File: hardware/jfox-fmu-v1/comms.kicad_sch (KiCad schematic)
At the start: 6 parts, among them J30 USB-C, J31 microSD, U30 TCAN332, U31 TCAN332

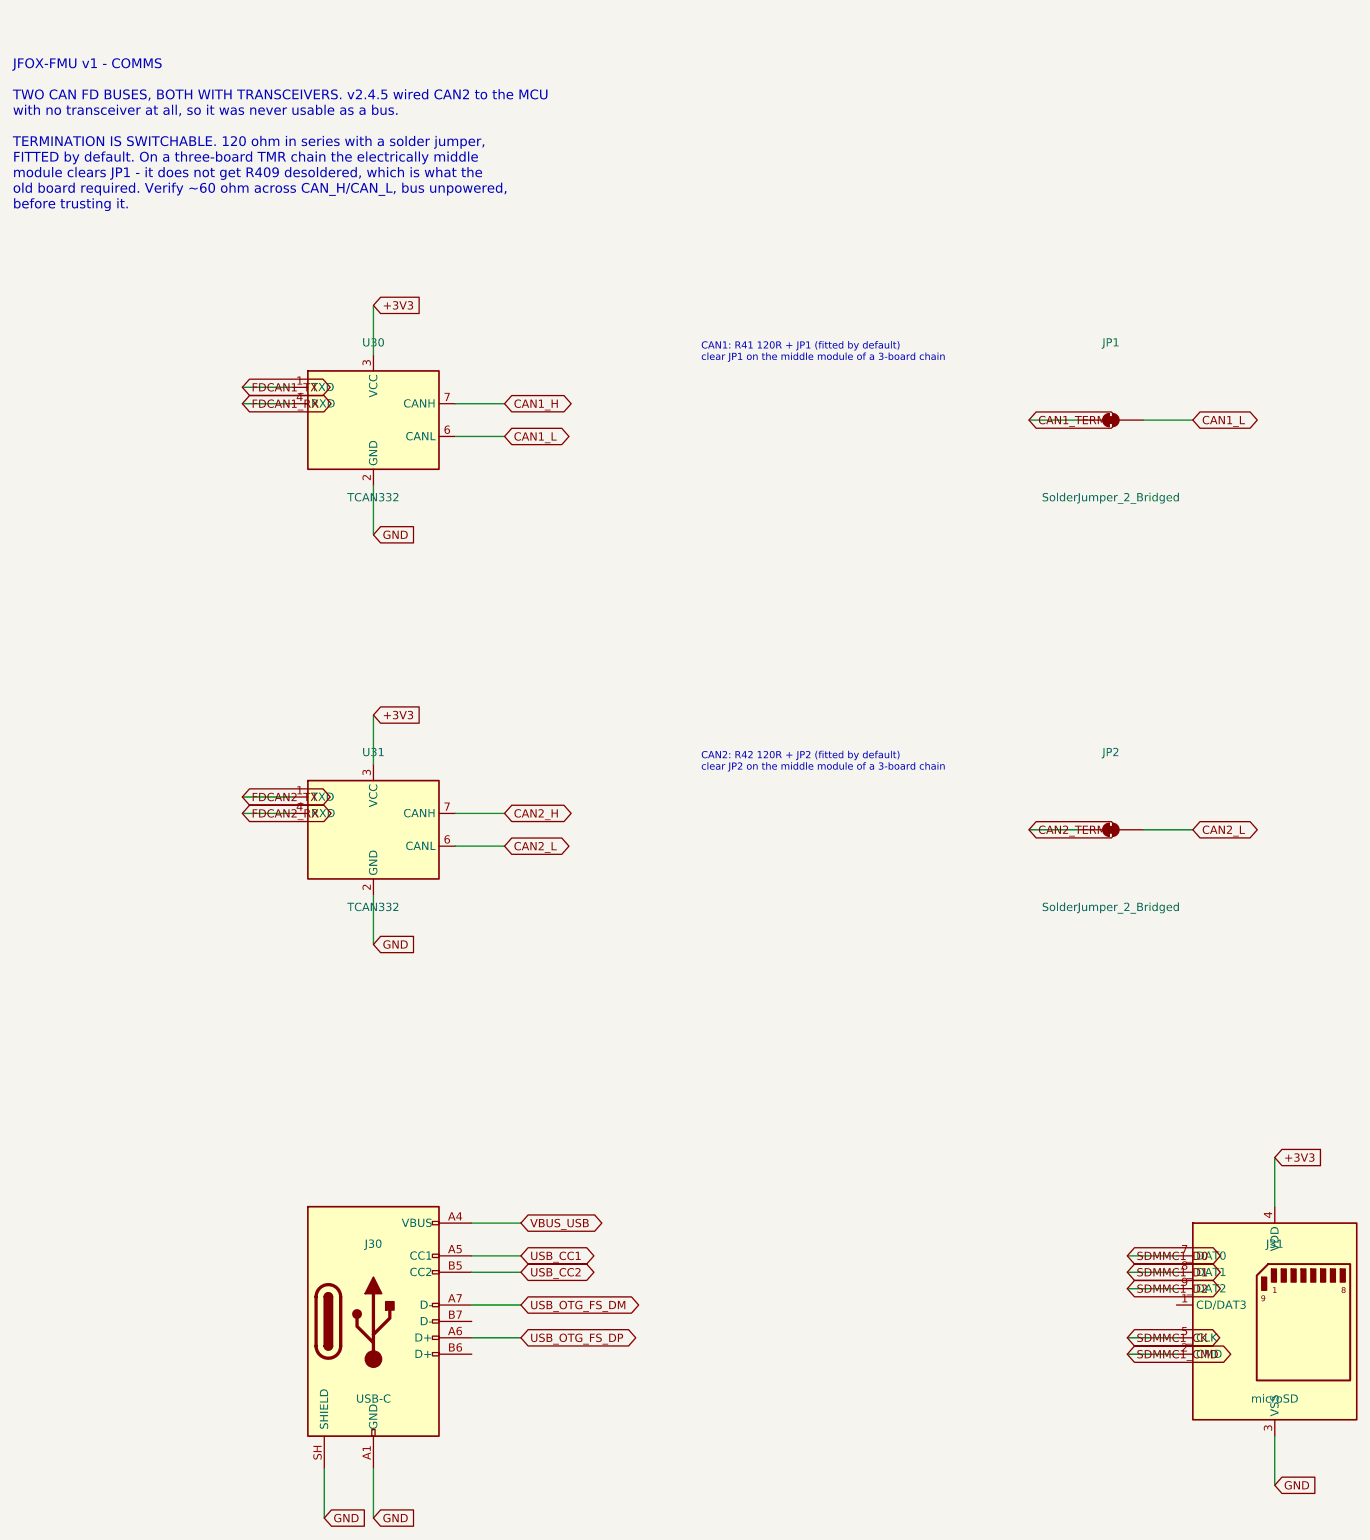
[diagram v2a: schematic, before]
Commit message: A4 title-blocked sheets, and the 25 power pins that were never wired
Every sheet now carries a title block naming JFOX Aircraft Co., Ltd., with a
per-sheet title, revision, date and the notes that used to float as loose text.

A4 PORTRAIT, not landscape, and not by preference. The STM32H753IITx symbol is
a single unit - KiCad's library gives it only _0_1 body and _1_1 pin
sub-symbols, so it cannot be split across pages - and its 176 pins span
231.1 mm. A4 landscape offers about 180 mm of usable height and would cut the
MCU in half. Portrait offers 237 mm. The part fits with 2 mm to spare, which
is why the page margin is 2 mm: it is the largest margin that still holds an
LQFP176, not a number chosen for looks.

The frame geometry was measured, not assumed - an empty A4 portrait sheet
plotted through kicad-cli, frame read off the SVG at 12,12 -> 198,285 with the
title block claiming x >= 90, y >= 253.

Three defects the work surfaced, in rising order of how much they mattered:

Every sheet had content at negative coordinates, off the page entirely, where
KiCad edits it happily and the plotter crops it away. Nothing had complained
because nothing was looking. fit() now translates each sheet into the drawable
area and refuses - loudly - to emit one that does not fit, because a schematic
that is silently cropped lies about the board.

fit() then passed the power sheet while its rightmost label sat 8.6 mm past
the frame. A global label's angle is the direction its CONNECTION faces, so
the text runs the opposite way; reading it the intuitive way put every
estimated extent on the wrong side of its anchor. That is worse than not
estimating: it reports "inside the frame" precisely when labels hang off it.
Caught by measuring KiCad's own plotted geometry instead of trusting the
estimate - which is what check_fmu_sheets.py now does on every sheet, with
--exclude-drawing-sheet so only the circuit is measured.

And centring the sheets by (SAFE_W - w) / 2 shifted every wire off th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
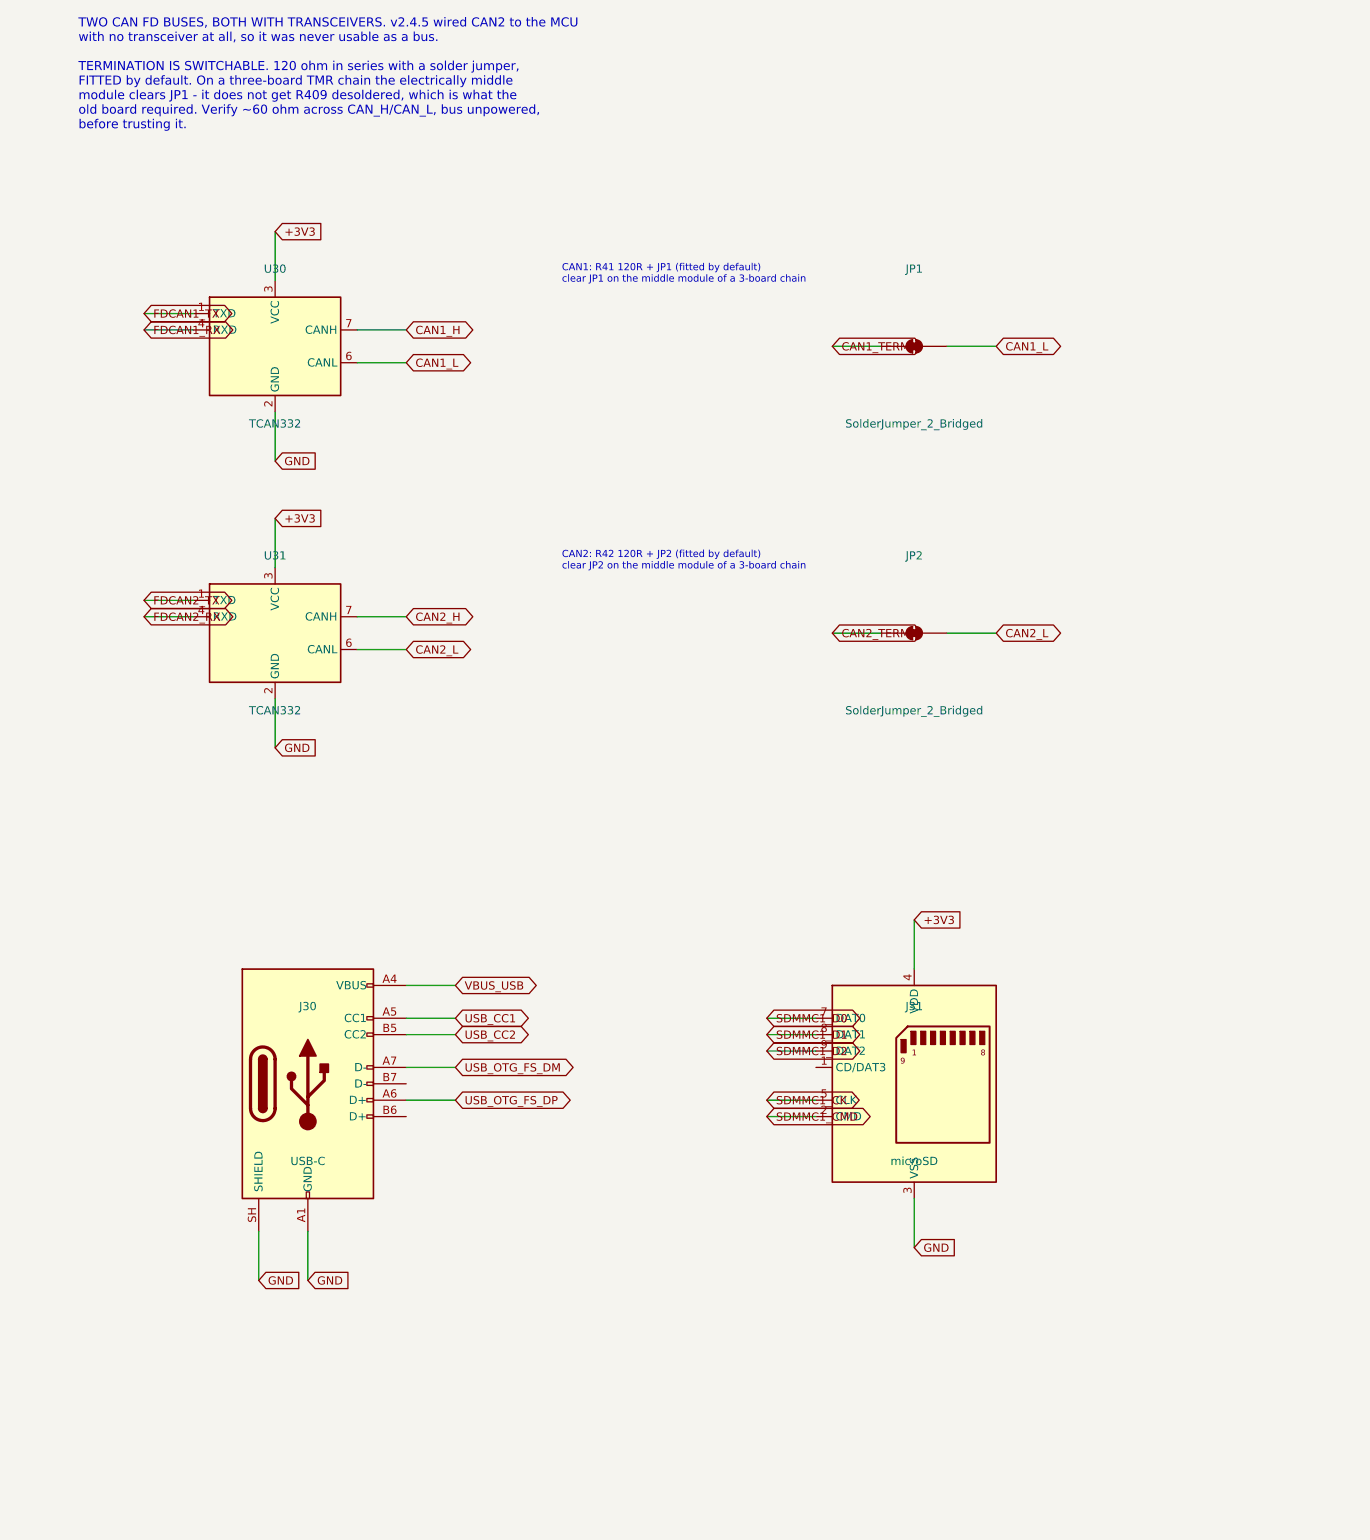
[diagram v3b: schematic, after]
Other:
- note added: "TWO CAN FD BUSES, BOTH WITH TRANSCEIVERS. v2.4.5 wired CAN2 to the MCU with no transceiver at all, so it was never usable as a bus. TERMINATION IS SWITCHABLE. 120 ohm in series with a solder jumper, FITTED by default. On a three-board TMR chain the electrically middle module clears JP1 - it does not get R409 desoldered, which is what the old board required. Verify ~60 ohm across CAN_H/CAN_L, bus 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"
- note removed: "JFOX-FMU v1 - COMMS TWO CAN FD BUSES, BOTH WITH TRANSCEIVERS. v2.4.5 wired CAN2 to the MCU with no transceiver at all, so it was never usable as a bus. TERMINATION IS SWITCHABLE. 120 ohm in series with a solder jumper, FITTED by default. On a three-board TMR chain the electrically middle module clears JP1 - it does not get R409 desoldered, which is what the old board required. Verify ~60 ohm acro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"
- company: (none) -> JFOX Aircraft Co., Ltd.
- title: (none) -> Comms and Storage

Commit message: Footprint every part, and verify each one exists
58 of 58 components now carry a footprint chosen against the package its
datasheet specifies, and check_fmu_footprints.py confirms every name resolves
to a file on disk.

Three of the names this design was carrying did not. The symbol library named
`Sensor_Motion:InvenSense_QFN-14_3x3mm_P0.5mm` and
`Sensor_Pressure:Bosch_LGA-10_2x2mm_P0.35mm`, neither of which is a footprint
in any installed library - both plausible, both fiction. The third was worse:
`Package_LGA:Bosch_LGA-14_3x2.5mm_P0.5mm` is real, matches the InvenSense
package on every word of its name, and is drawn for the BMI160 with 0.675 mm
pads where InvenSense wants 0.475 mm.

Notable choices, each traceable:
  LTC4417CGN  GN is the 16-lead narrow SSOP.
  TPS62132    RGT 3x3 VQFN. TI's land drawing (4222419/E) gives the exposed
              pad as 1.55 mm; KiCad's 1.6 mm variant is closest. Thermal-via
              variant, since the datasheet is explicit that the pad must be
              soldered and that dissipation limits output power.
  Bulk caps   4u7/10u/22u get an 0805, not the 0402 every other capacitor
              gets. Assigning one size to all of them produces a board that
              cannot be built from the BOM it ships with.
  L1          a generic 1210 land, and labelled as such - the 2.2 uH part is
              not chosen yet, since saturation current and DCR still have to
              be picked against the real 550 mA peak.

The checker was wrong on its first run, in a way worth recording because the
failure mode is self-concealing. It matched ref, value and footprint in one
regex with the footprint group optional, so a component with no footprint -
precisely what it exists to find - failed to match at all, dropped out of the
list, and the run reported "every component maps to a footprint" while the
count quietly fell by one. A check whose failure mode is to stop seeing the
failure is worse than no check. Now it splits into per-com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
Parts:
- J30: footprint (none) -> Connector_USB:USB_C_Receptacle_GCT_USB4085
- J31: footprint (none) -> Connector_Card:microSD_HC_Hirose_DM3AT-SF-PEJM5
- JP1, JP2: footprint (none) -> Jumper:SolderJumper-2_P1.3mm_Bridged_Pad1.0x1.5mm
- U30, U31: footprint (none) -> Package_SO:SOIC-8_3.9x4.9mm_P1.27mm
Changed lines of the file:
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@@
+		)
+		)
+		(property "Footprint" "Package_SO:SOIC-8_3.9x4.9mm_P1.27mm"
+			(at 60.96 64.77 0)
+			(hide yes)
+			(effects
+			(font
+				(size 1.27 1.27)
+			)
 		)
 		)
 		(instances
 			(project "jfox-fmu"
-				(path "/8995d84e-e54d-4399-8a49-bdf850cff689"
+				(path "/a1deec84-f86e-41a2-b546-78f7ca11e72e"
 					(reference "U30")
 					(unit 1)
@@
 		)
 		)
+		(property "Footprint" "Jumper:SolderJumper-2_P1.3mm_Bridged_Pad1.0x1.5mm"
+			(at 160.02 64.77 0)
+			(hide yes)
+			(effects
+			(font
+				(size 1.27 1.27)
+			)
+		)
+		)
 		(instances
 			(project "jfox-fmu"
-				(path "/8995d84e-e54d-4399-8a49-bdf850cff689"
+				(path "/a1deec84-f86e-41a2-b546-78f7ca11e72e"
 					(reference "JP1")
 					(unit 1)
@@
 		)
 		)
+		(property "Footprint" "Package_SO:SOIC-8_3.9x4.9mm_P1.27mm"
+			(at 60.96 109.22 0)
+			(hide yes)
+			(effects
+			(font
+				(size 1.27 1.27)
+			)
+		)
+		)
 		(instances
 			(project "jfox-fmu"
-				(path "/8995d84e-e54d-4399-8a49-bdf850cff689"
+				(path "/a1deec84-f86e-41a2-b546-78f7ca11e72e"
 					(reference "U31")
 					(unit 1)
@@
 		)
 		)
+		(property "Footprint" "Jumper:SolderJumper-2_P1.3mm_Bridged_Pad1.0x1.5mm"
+			(at 160.02 109.22 0)
+			(hide yes)
+			(effects
+			(font
+				(size 1.27 1.27)
+			)
+		)
+		)
 		(instances
 			(project "jfox-fmu"
-				(path "/8995d84e-e54d-4399-8a49-bdf850cff689"
+				(path "/a1deec84-f86e-41a2-b546-78f7ca11e72e"
 					(reference "JP2")
 					(unit 1)
@@
 		)
 		)
+		(property "Footprint" "Connector_USB:USB_C_Receptacle_GCT_USB4085"
+			(at 66.04 179.07 0)
+			(hide yes)
+			(effects
+			(font
+				(size 1.27 1.27)
+			)
+		)
+		)
 		(instances
 			(project "jfox-fmu"
-				(path "/8995d84e-e54d-4399-8a49-bdf850cff689"
+				(path "/a1deec84-f86e-41a2-b546-78f7ca11e72e"
 					(reference "J30")
 					(unit 1)
@@
 		)
 		)
+		(property "Footprint" "Connector_Card:microSD_HC_Hirose_DM3AT-SF-PEJM5"
+			(at 160.02 179.07 0)
+			(hide yes)
+			(effects
+			(font
+				(size 1.27 1.27)
+			)
+		)
+		)
 		(instances
 			(project "jfox-fmu"
-				(path "/8995d84e-e54d-4399-8a49-bdf850cff689"
+				(path "/a1deec84-f86e-41a2-b546-78f7ca11e72e"
 					(reference "J31")
 					(unit 1)
